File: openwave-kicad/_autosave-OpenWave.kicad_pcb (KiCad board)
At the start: 2 copper layers, 51 parts, among them IC1 STM32F405RGT, J1 USB_OTG, J2 503182-1852, J3 Screw_Terminal_01x04, J4 Conn_01x04_Female, U1 MIC5239-3.3YS, U2 MIC5209-4.2, U3 BNO055, U4 MAX3232, Y1 8MHz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

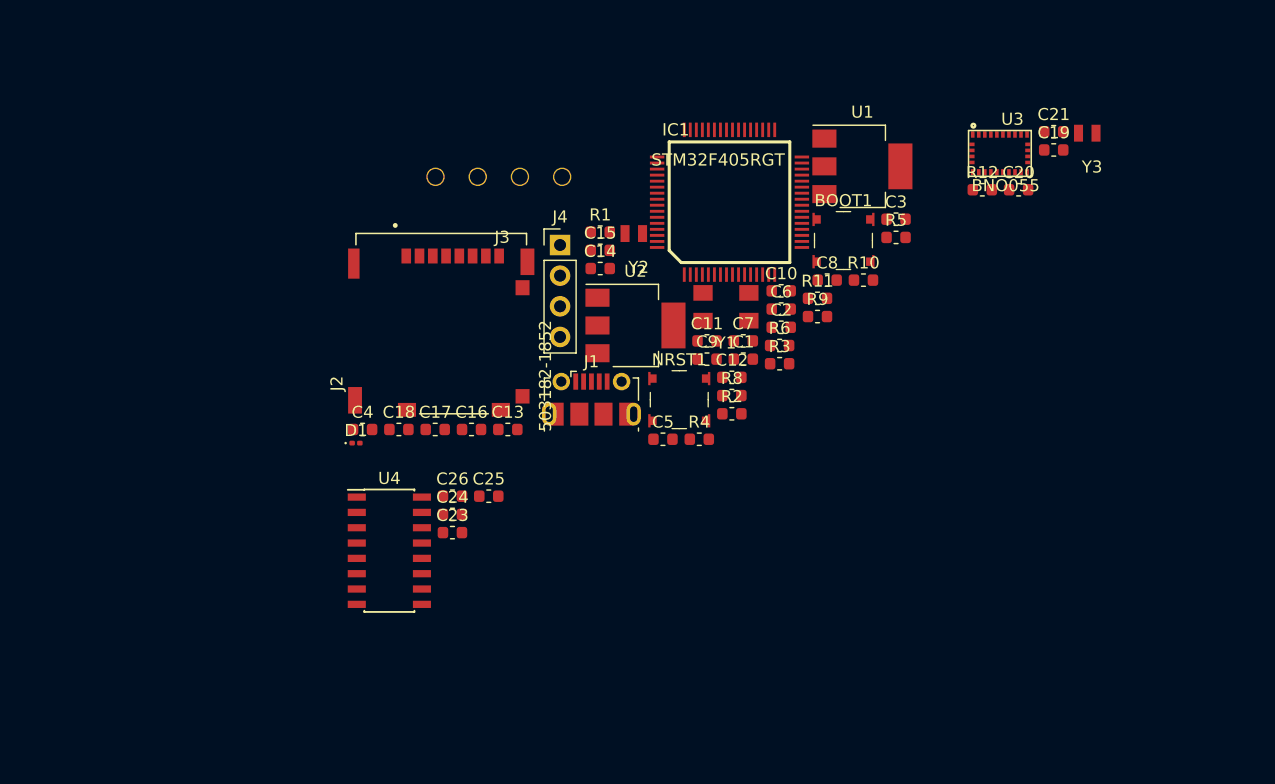
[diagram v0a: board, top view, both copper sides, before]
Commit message: linked all footprints to symbols, ready for routing
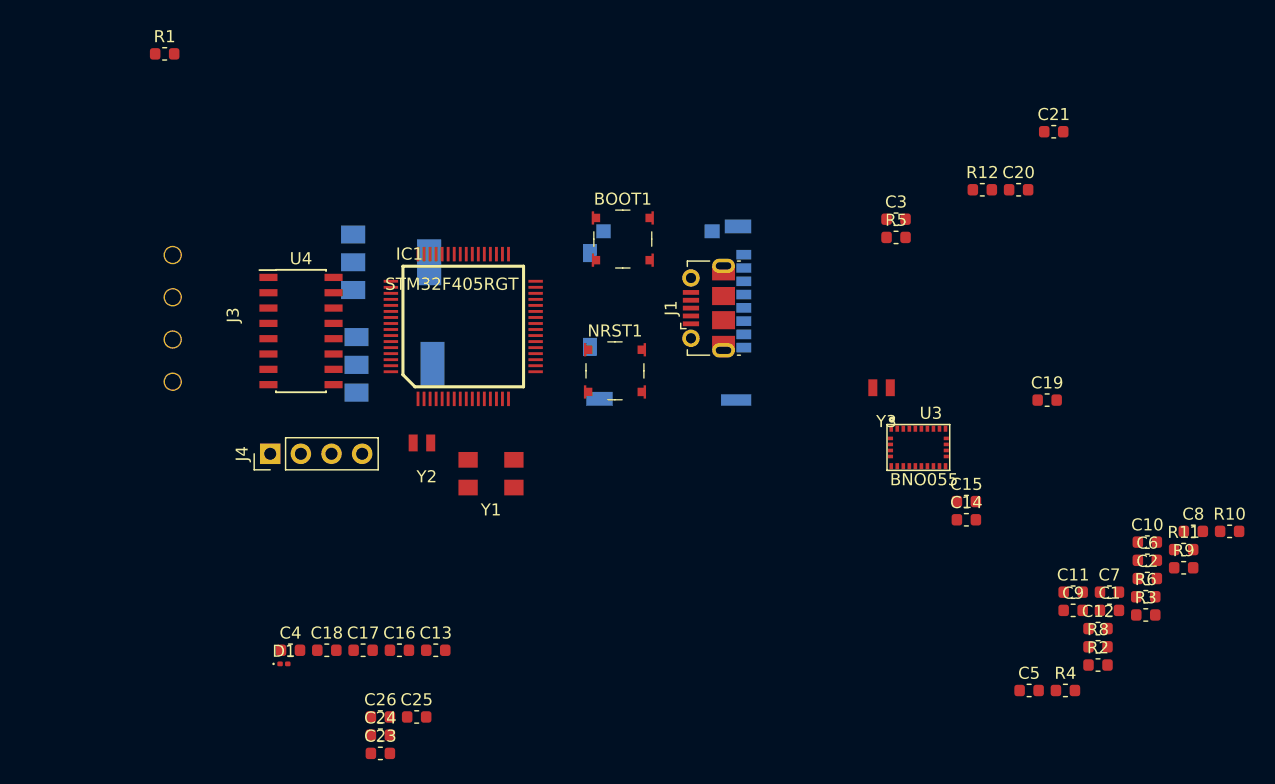
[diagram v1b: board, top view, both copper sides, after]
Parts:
- J2, U1, U2: moved to B.Cu
- moved J3 43.7 mm to (72.0, 64.7), turned to 90 degrees
- moved U1 42.1 mm to (94.6, 80.8)
- moved R1 39.0 mm to (75.6, 55.0)
- moved C7 36.8 mm to (153.9, 99.6)
- moved R3 36.8 mm to (156.9, 101.5)
- moved R6 36.8 mm to (156.9, 100.0)
- moved C1 36.8 mm to (153.9, 101.1)
- moved R4 36.8 mm to (150.2, 107.8)
- moved C10 36.8 mm to (157.0, 95.5)
- moved C11 36.8 mm to (150.9, 99.6)
- moved C12 36.8 mm to (152.9, 102.6)
- moved C14 36.8 mm to (142.0, 93.6)
- moved C15 36.8 mm to (142.0, 92.1)
- moved C2 36.8 mm to (157.0, 98.5)
- moved C6 36.8 mm to (157.0, 97.0)
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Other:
- copper layers 2 -> 4

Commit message: fixed unconnected nets, routing 15% done
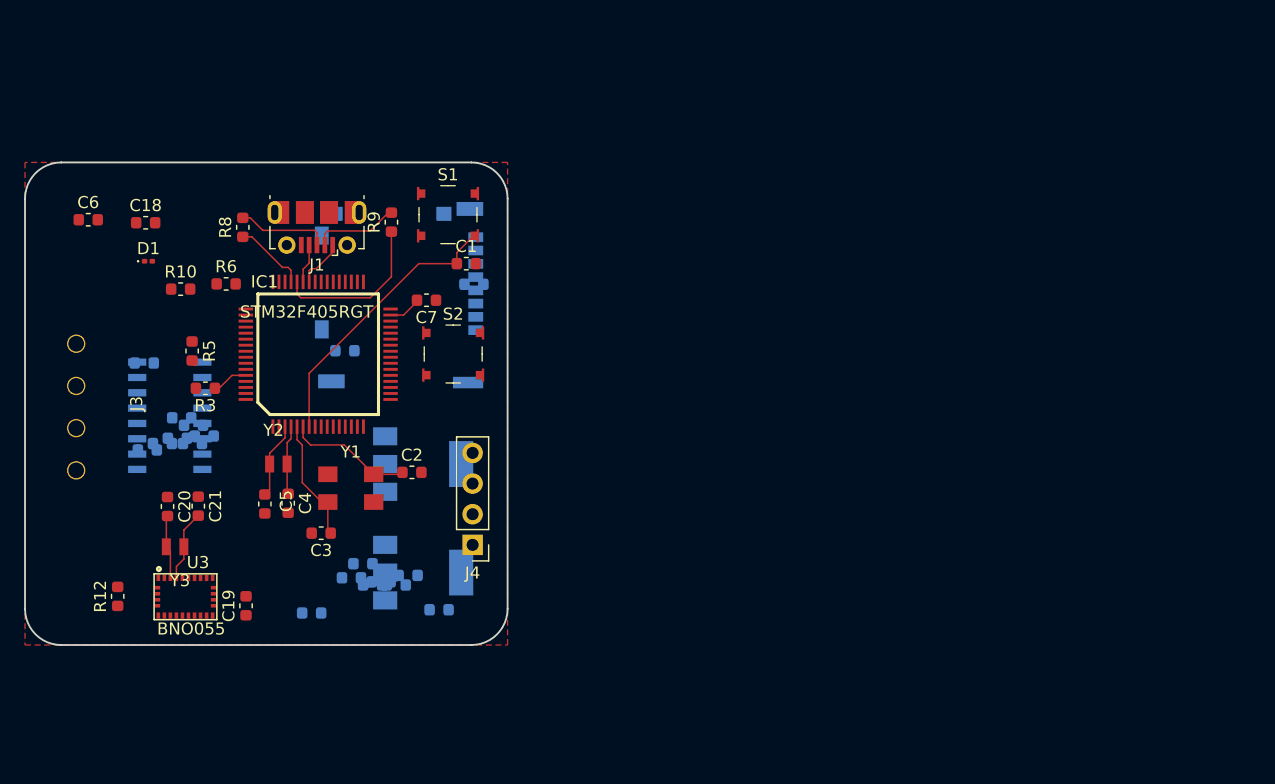
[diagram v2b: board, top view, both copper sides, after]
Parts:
- removed BOOT1, NRST1: SW_Push, digikey-footprints:Switch_Tactile_SMD_4.5x4.5mm_TL3315NF160Q
- added S1: TL3315NF160Q, digikey-footprints:Switch_Tactile_SMD_4.5x4.5mm_TL3315NF160Q, F.Cu at (99.1, 68.3)
- added S2: TL3315NF160Q, digikey-footprints:Switch_Tactile_SMD_4.5x4.5mm_TL3315NF160Q, F.Cu at (99.5, 79.9)
- C10, C11, C12, C13, C14, C15, C16, C17, C23, C24, C25, C26, C8, C9, R1, R11, R2, R4, U4: moved to B.Cu
- moved C6 92.2 mm to (69.2, 68.8)
- moved R10 89.2 mm to (76.9, 74.5)
- moved R11 82.6 mm to (77.9, 87.3)
- moved R6 80.5 mm to (80.7, 74.1)
- moved R3 80.2 mm to (79.0, 82.7), turned to 180 degrees
- moved R12 79.2 mm to (71.7, 100.0), turned to 90 degrees
- moved R8 79.0 mm to (82.0, 69.4), turned to 90 degrees
- moved C10 78.7 mm to (78.8, 86.7)
- moved C21 77.4 mm to (78.4, 92.5), turned to 270 degrees
- moved C20 75.3 mm to (75.8, 92.5), turned to 270 degrees
- moved R9 71.6 mm to (94.4, 69.0), turned to 90 degrees
- moved C19 68.6 mm to (82.3, 100.8), turned to 90 degrees
- moved C8 67.5 mm to (93.5, 98.8)
- moved C14 65.7 mm to (76.6, 86.9)
- moved C5 65.2 mm to (83.9, 92.3), turned to 270 degrees
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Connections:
- J4 pad 3: /TX2 -> /IO_PB10
- J4 pad 4: /RX2 -> /IO_PB11
- U4 pad 11: /STM_TX3 -> /IO_PA2
- U4 pad 12: /STM_RX3 -> /IO_PA3
- Y2 pad 2: Net-(Y2-Pad2) -> /N$5
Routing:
- net /NRST: track 0.00 -> 23.3 mm
- net /FS_DM: track 0.00 -> 13.4 mm
- net /N$9: track 0.00 -> 10.5 mm
- net /N$10: track 0.00 -> 10.3 mm
- net Net-(J1-Pad3): track 0.00 -> 7.68 mm
- net Net-(J1-Pad2): track 0.00 -> 7.18 mm
- net /N$5: track 0.00 -> 6.32 mm
- net /FS_DP: track 0.00 -> 6.11 mm
- net /BNO055/XOUT32: track 0.00 -> 5.91 mm
- net /N$6: track 0.00 -> 5.73 mm
- net /BNO055/XIN32: track 0.00 -> 5.31 mm
- net +5V: track 0.00 -> 4.12 mm
- net /FS_USB_ID: track 0.00 -> 3.26 mm
- net /BOOT0: track 0.00 -> 3.01 mm
- net /N$2: track 0.00 -> 2.77 mm
- added copper zone on F.Cu, net GND
- added copper zone on GND, net GND
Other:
- board outline added: 40 x 40 mm
- net class Default: clearance 0.2 -> 0.127
- rule trace_clearance: 0.2 -> 0.127
- rule trace_min: 0.2 -> 0.127
- rule via_min_drill: 0.3 -> 0.254
